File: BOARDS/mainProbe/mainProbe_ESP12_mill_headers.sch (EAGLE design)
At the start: 10 parts

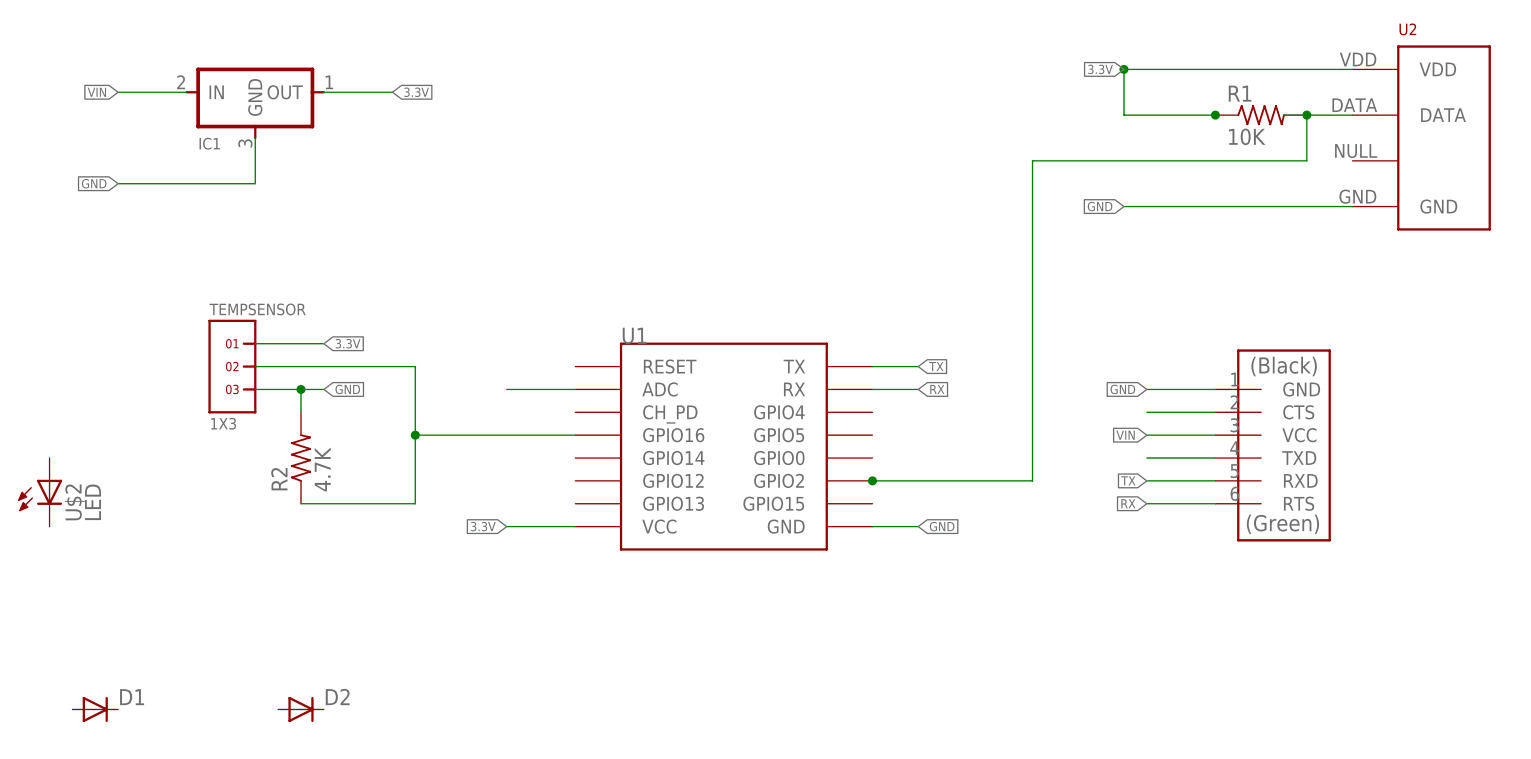
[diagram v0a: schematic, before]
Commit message: placa com headers thanks to FS
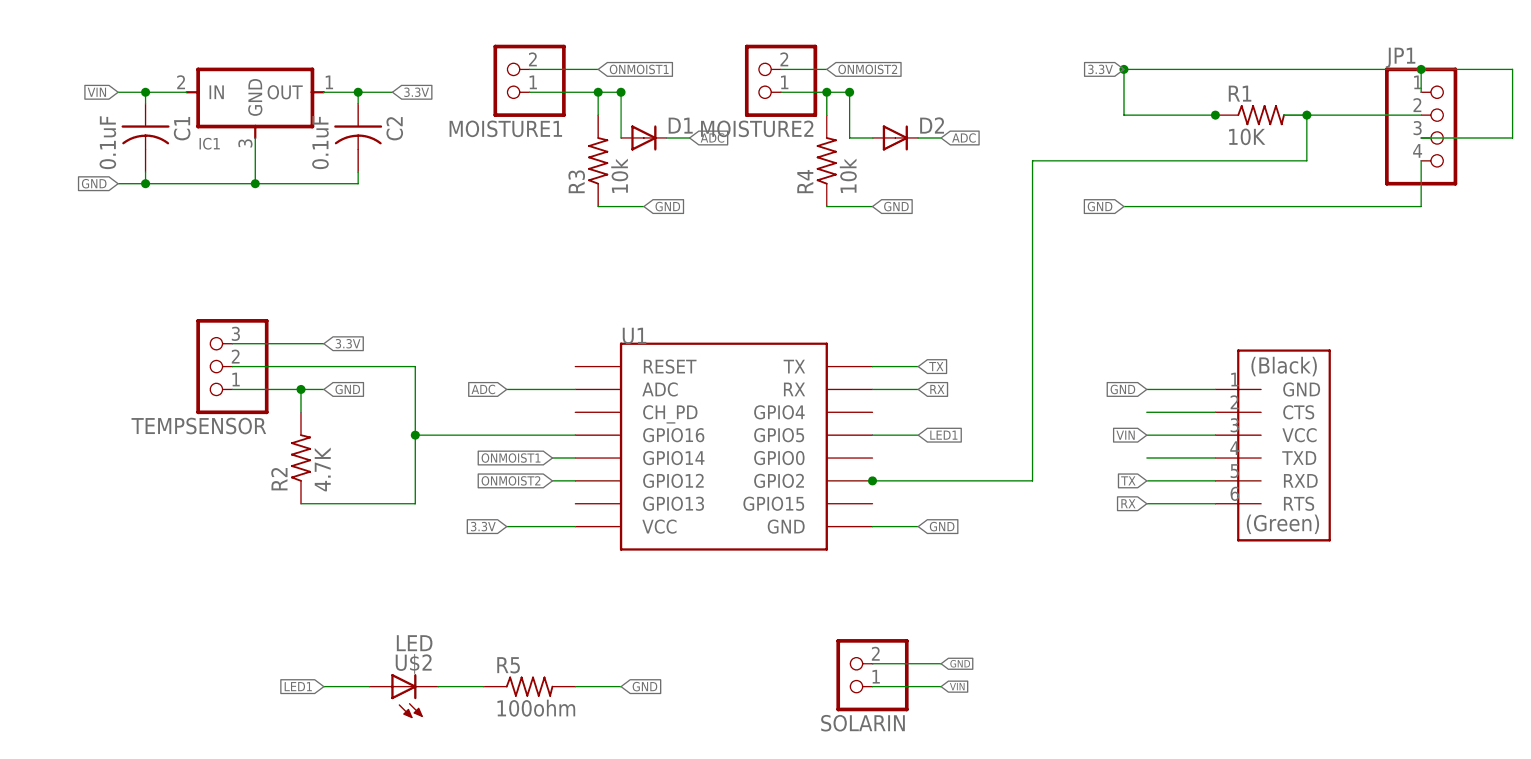
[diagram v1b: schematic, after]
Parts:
- removed U2: (no value), RHT03_DHT-22_AM2302:RHT03_DHT-22_AM2302
- added C1, C2: 0.1uF, fab:CAP-US1206
- added JP1: (no value), pinhead:PINHD-1X4
- added MOISTURE1, MOISTURE2: (no value), pinhead:PINHD-1X2
- added R3, R4: 10k, fab:RES-US1206
- added R5: 100ohm, fab:RES-US1206
- added SOLARIN: (no value), pinhead:PINHD-1X2/90
- TEMPSENSOR: value 1X3 -> (none); device headers(2mm):1X3 -> pinhead:PINHD-1X3
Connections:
- removed net N$12: U1.ADC
- new net ADC: D1.C, D2.C, U1.ADC
- new net LED1: U$2.A, U1.GPIO5
- new net N$5: D1.A, MOISTURE1.1, R3.2
- new net N$6: R5.1, U$2.C
- new net N$7: D2.A, MOISTURE2.1, R4.2
- new net ONMOIST1: MOISTURE1.2, U1.GPIO14
- new net ONMOIST2: MOISTURE2.2, U1.GPIO12
- net 3.3V: now also C2.1, JP1.1, JP1.3, TEMPSENSOR.3; no longer TEMPSENSOR.1, U2.VDD
- net GND: now also C1.2, C2.2, JP1.4, R3.1, R4.1, R5.2, SOLARIN.2, TEMPSENSOR.1; no longer TEMPSENSOR.3, U2.GND
- net N$8: now also JP1.2; no longer U2.DATA
- net VIN: now also C1.1, SOLARIN.1
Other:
- moved on the sheet: D1, D2, U$2
